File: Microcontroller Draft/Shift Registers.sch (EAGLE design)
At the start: 20 parts, among them IC1 74HC595N, IC2 74HC595N

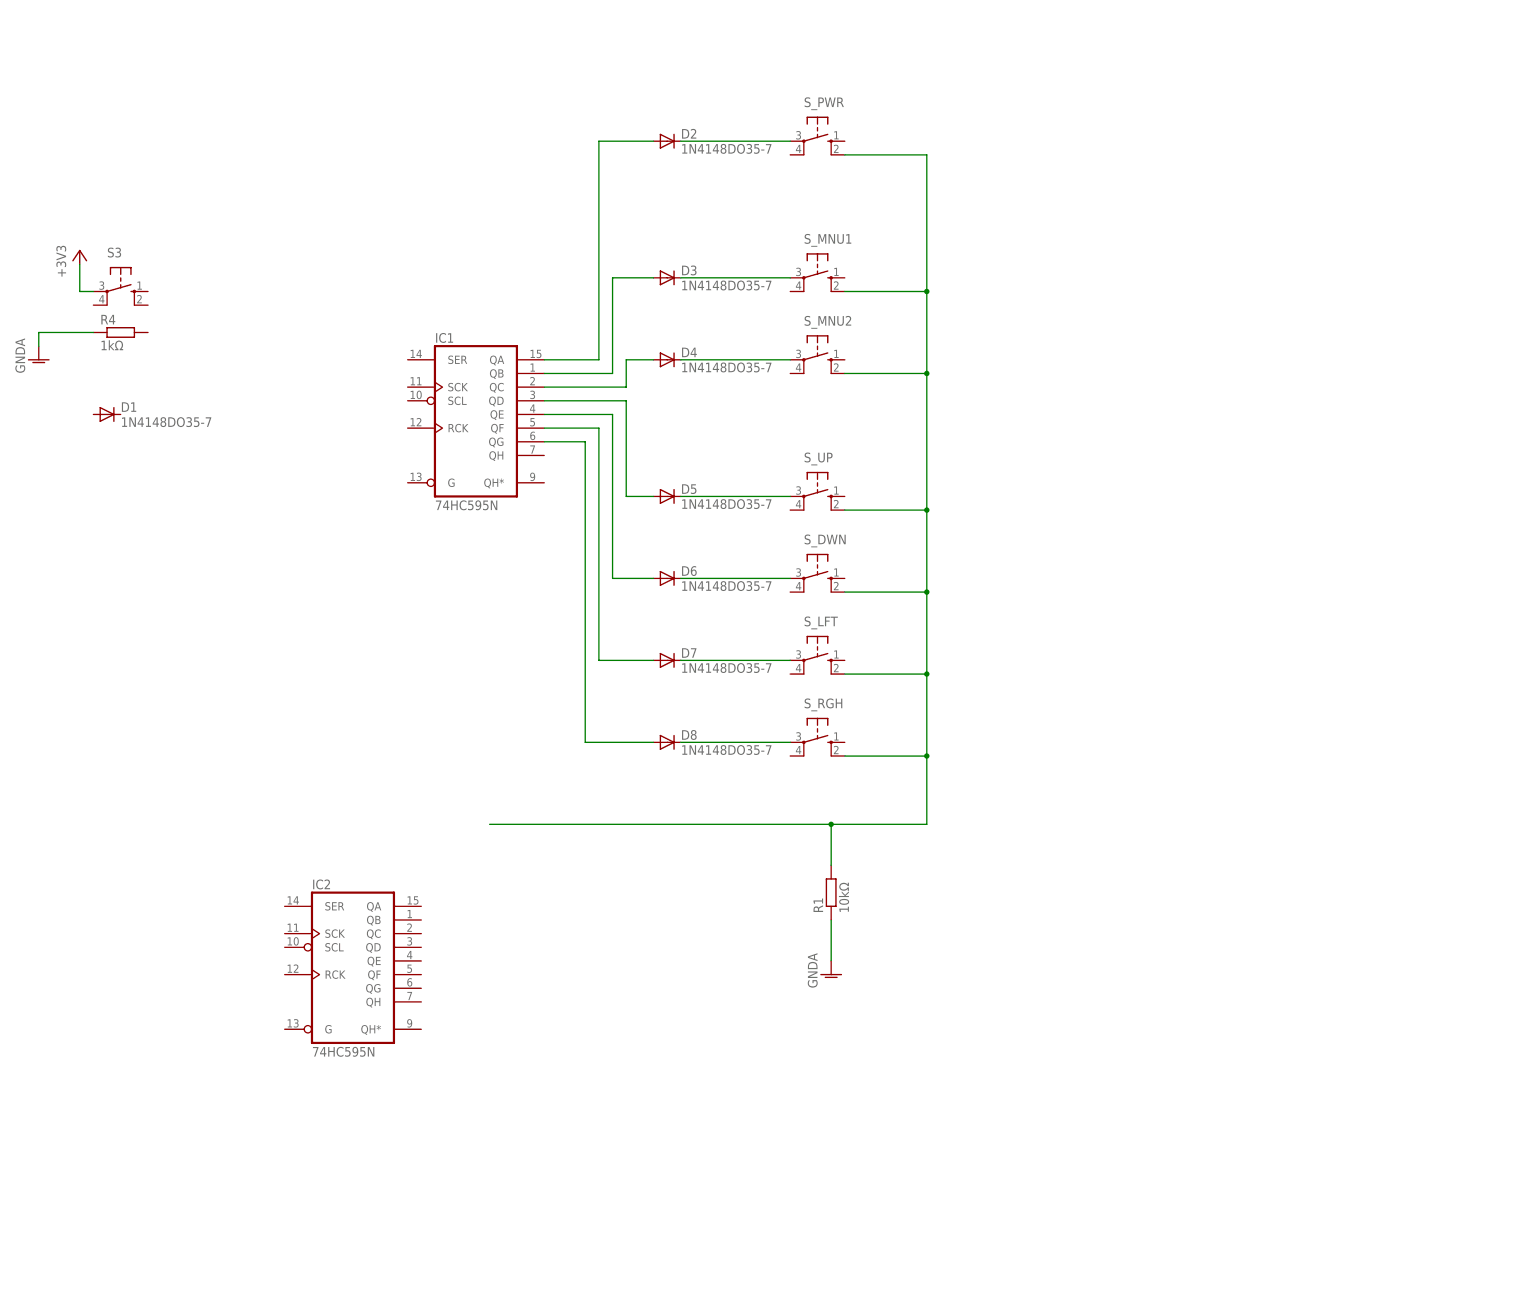
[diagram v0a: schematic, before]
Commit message: Finished the shift register oriented design schematic
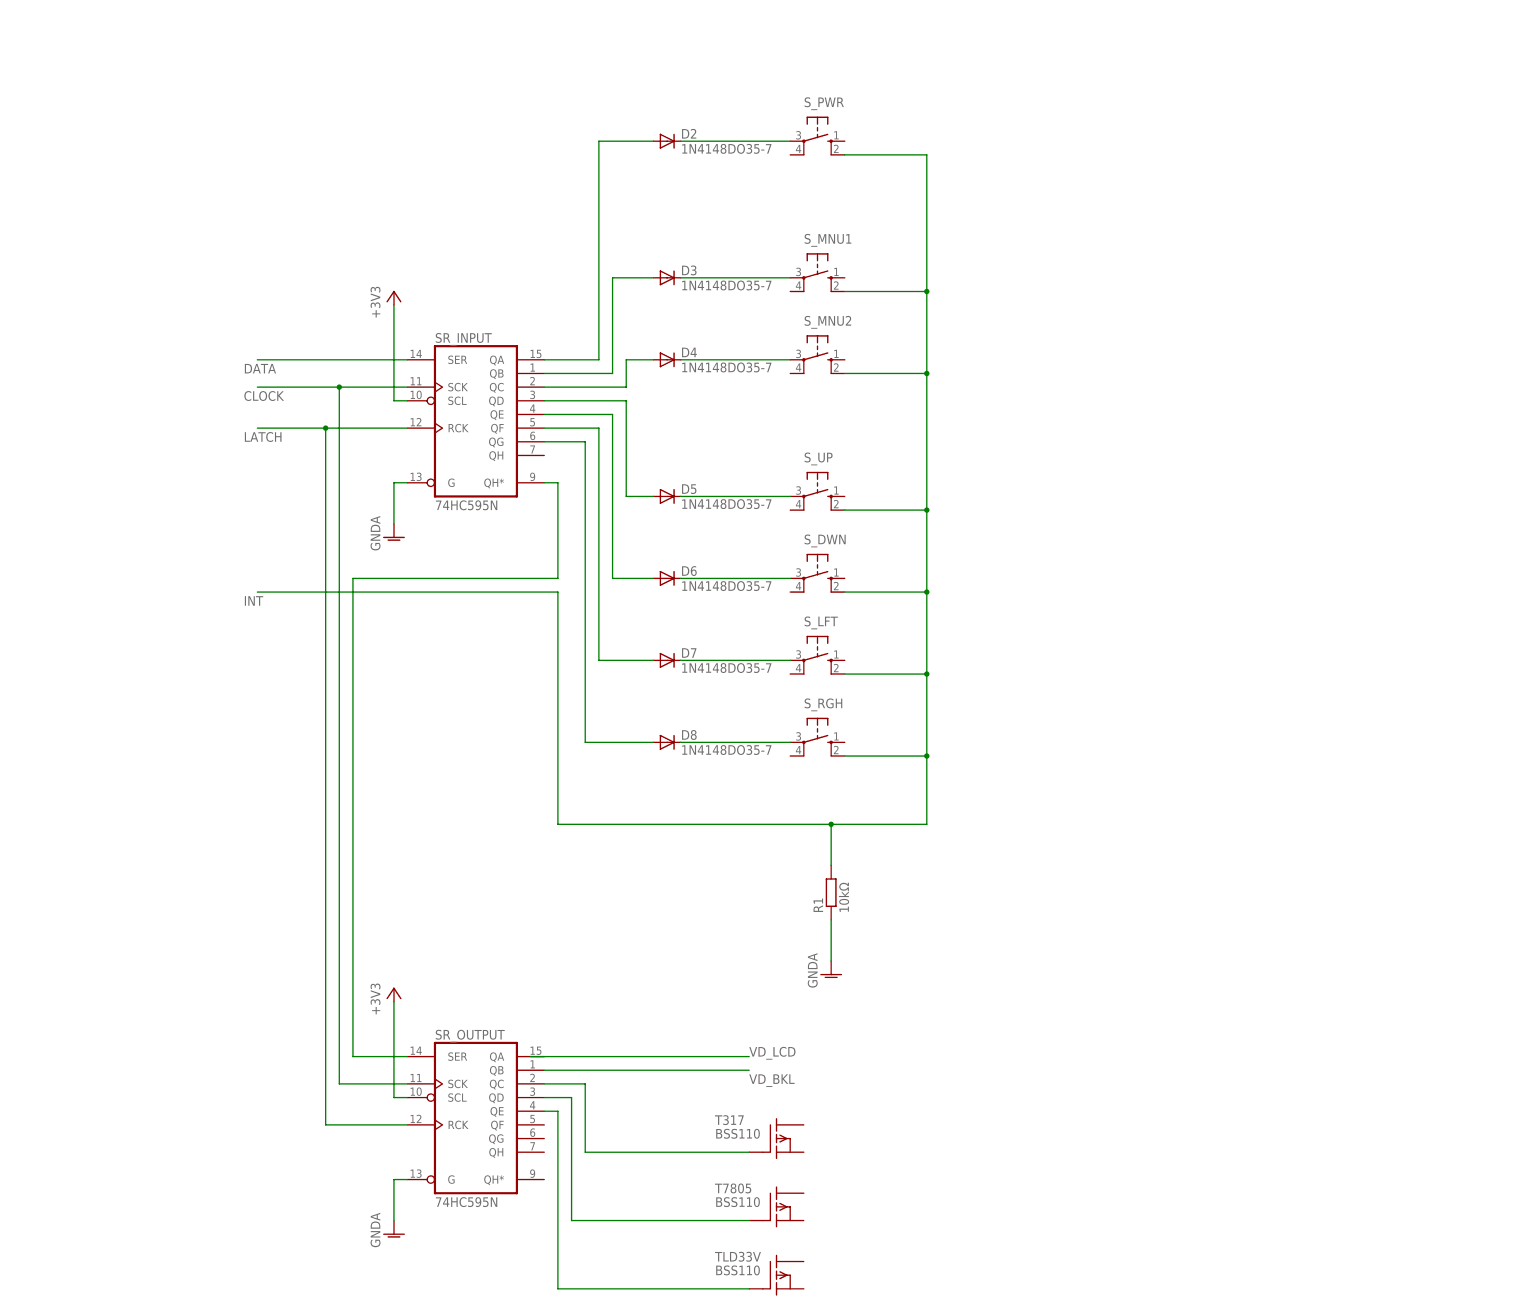
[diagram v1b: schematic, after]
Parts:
- removed D1: 1N4148DO35-7, diode:1N4148DO35-7
- removed IC2: 74HC595N, 74xx-eu:74HC595N
- removed R4: 1kΩ, resistor:R-EU_0207/10
- removed S3: (no value), switch-omron:10-XX
- added SR_OUTPUT: 74HC595N, 74xx-eu:74HC595N
- added T317, T7805, TLD33V: BSS110, transistor-fet:BSS110
- renumbered IC1 to SR_INPUT
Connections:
- net N$1 renamed INT
- new net CLOCK: SR_INPUTA.SCK, SR_OUTPUTA.SCK
- new net DATA: SR_INPUTA.SER
- new net LATCH: SR_INPUTA.RCK, SR_OUTPUTA.RCK
- new net N$19: SR_OUTPUTA.QE, TLD33V.G
- new net N$20: SR_OUTPUTA.QD, T7805.G
- new net N$21: SR_OUTPUTA.QC, T317.G
- new net N$22: SR_INPUTA.QH*, SR_OUTPUTA.SER
- new net VD_BKL: SR_OUTPUTA.QB
- new net VD_LCD: SR_OUTPUTA.QA
- net +3V3: now also SR_INPUTA.SCL, SR_OUTPUTA.SCL; no longer S3.P
- net GNDA: now also SR_INPUTA.G, SR_OUTPUTA.G; no longer R4.1

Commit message: Added some decoupling capacitors
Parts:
- added C1, C7: 0.1uF, rcl:C-EU025-025X050
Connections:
- net +3V3: now also C1.2, C7.2
- net GNDA: now also C1.1, C7.1
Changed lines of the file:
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@@
 <part name="GND3" library="supply1" deviceset="GNDA" device=""/>
 <part name="+3V2" library="supply1" deviceset="+3V3" device=""/>
+<part name="C7" library="rcl" deviceset="C-EU" device="025-025X050" value="0.1uF"/>
+<part name="GND4" library="supply1" deviceset="GNDA" device=""/>
+<part name="C1" library="rcl" deviceset="C-EU" device="025-025X050" value="0.1uF"/>
+<part name="GND5" library="supply1" deviceset="GNDA" device=""/>
 </parts>
 <sheets>
@@
 <instance part="GND3" gate="1" x="-38.1" y="-58.42"/>
 <instance part="+3V2" gate="G$1" x="-38.1" y="-12.7"/>
+<instance part="C7" gate="G$1" x="-50.8" y="111.76" rot="R90"/>
+<instance part="GND4" gate="1" x="-55.88" y="109.22"/>
+<instance part="C1" gate="G$1" x="-58.42" y="-17.78" rot="R90"/>
+<instance part="GND5" gate="1" x="-63.5" y="-22.86"/>
 </instances>
 <busses>
@@
 <segment>
 <pinref part="+3V1" gate="G$1" pin="+3V3"/>
-<wire x1="-38.1" y1="114.3" x2="-38.1" y2="96.52" width="0.1524" layer="91"/>
+<wire x1="-38.1" y1="114.3" x2="-38.1" y2="111.76" width="0.1524" layer="91"/>
 <pinref part="SR_INPUT" gate="A" pin="SCL"/>
+<wire x1="-38.1" y1="111.76" x2="-38.1" y2="96.52" width="0.1524" layer="91"/>
 <wire x1="-38.1" y1="96.52" x2="-35.56" y2="96.52" width="0.1524" layer="91"/>
+<pinref part="C7" gate="G$1" pin="2"/>
+<wire x1="-45.72" y1="111.76" x2="-38.1" y2="111.76" width="0.1524" layer="91"/>
+<junction x="-38.1" y="111.76"/>
 </segment>
 <segment>
@@
 <pinref part="+3V2" gate="G$1" pin="+3V3"/>
 <wire x1="-35.56" y1="-33.02" x2="-38.1" y2="-33.02" width="0.1524" layer="91"/>
-<wire x1="-38.1" y1="-33.02" x2="-38.1" y2="-15.24" width="0.1524" layer="91"/>
+<wire x1="-38.1" y1="-33.02" x2="-38.1" y2="-17.78" width="0.1524" layer="91"/>
+<pinref part="C1" gate="G$1" pin="2"/>
+<wire x1="-38.1" y1="-17.78" x2="-38.1" y2="-15.24" width="0.1524" layer="91"/>
+<wire x1="-53.34" y1="-17.78" x2="-38.1" y2="-17.78" width="0.1524" layer="91"/>
+<junction x="-38.1" y="-17.78"/>
 </segment>
 </net>
@@
 <wire x1="-38.1" y1="-48.26" x2="-38.1" y2="-55.88" width="0.1524" layer="91"/>
 </segment>
+<segment>
+<pinref part="C7" gate="G$1" pin="1"/>
+<wire x1="-53.34" y1="111.76" x2="-55.88" y2="111.76" width="0.1524" layer="91"/>
+<pinref part="GND4" gate="1" pin="GNDA"/>
+</segment>
+<segment>
+<pinref part="C1" gate="G$1" pin="1"/>
+<wire x1="-60.96" y1="-17.78" x2="-63.5" y2="-17.78" width="0.1524" layer="91"/>
+<pinref part="GND5" gate="1" pin="GNDA"/>
+<wire x1="-63.5" y1="-17.78" x2="-63.5" y2="-20.32" width="0.1524" layer="91"/>
+</segment>
 </net>

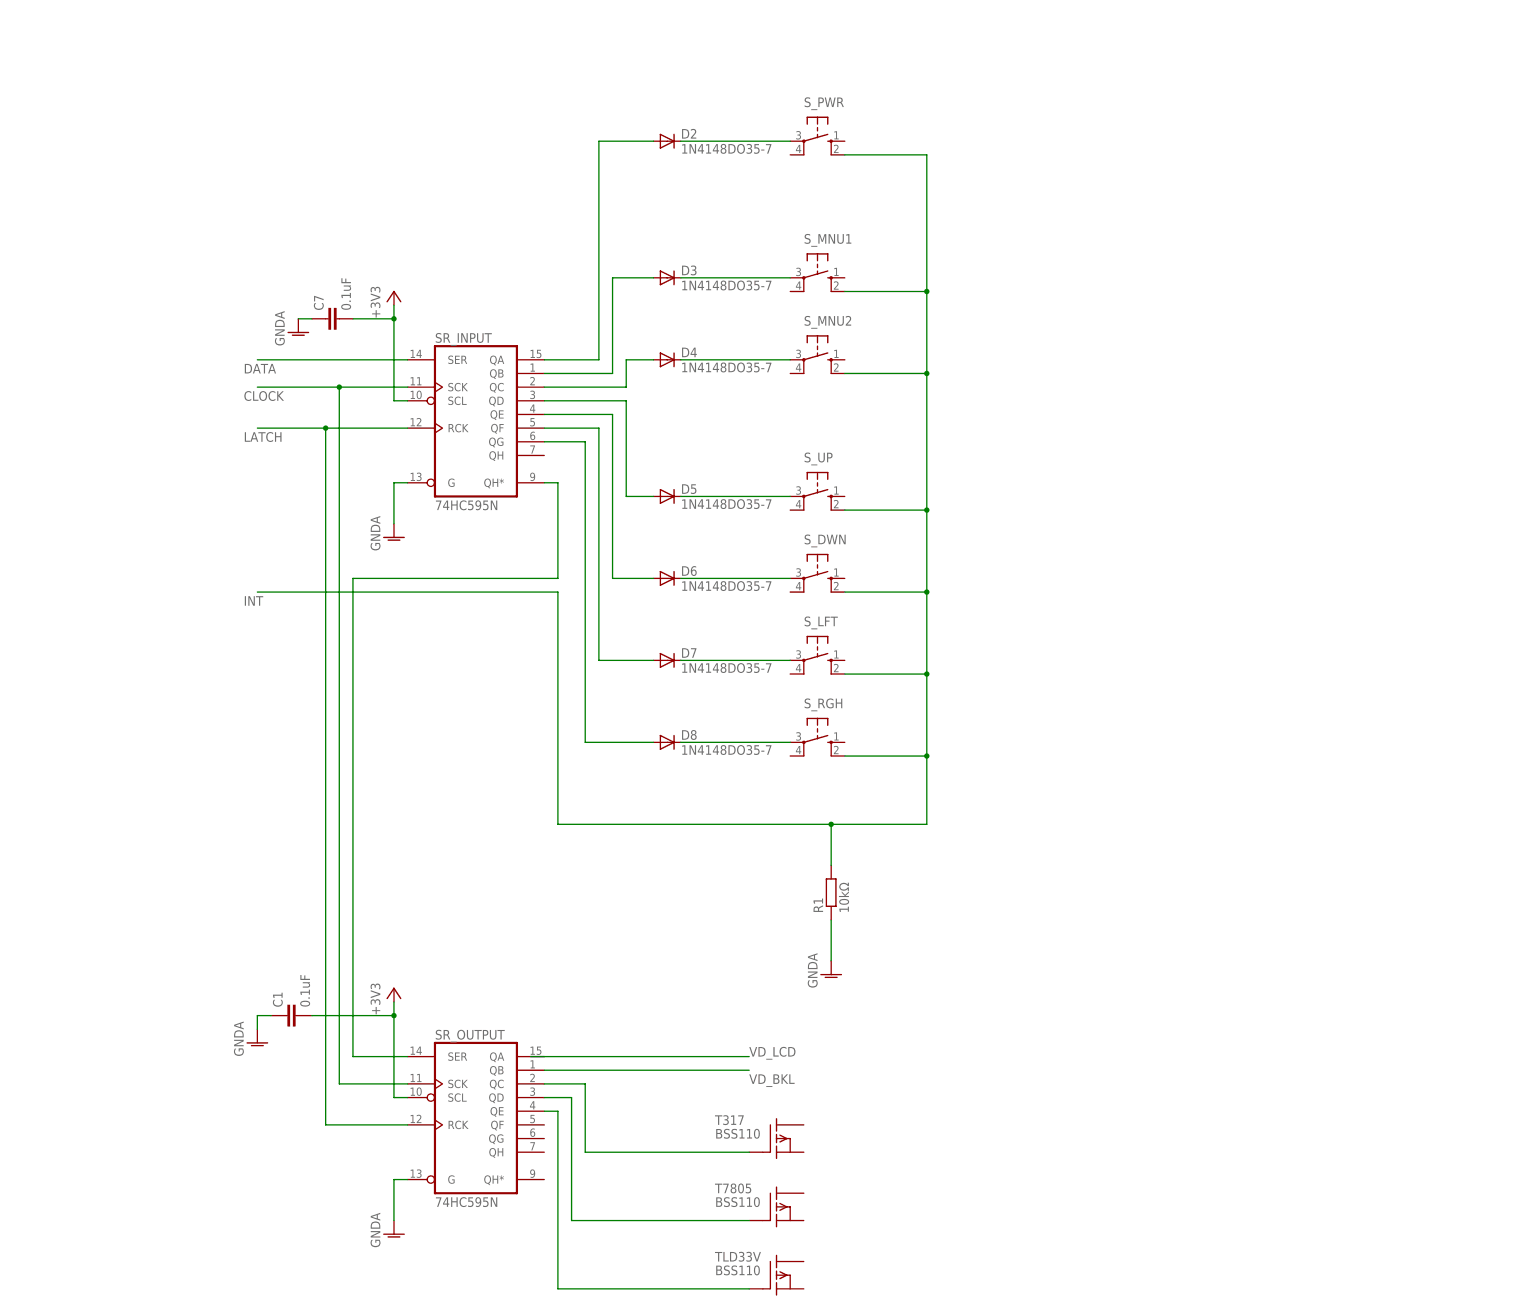
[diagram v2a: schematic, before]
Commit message: Improved the shift register design since we are going to use a rotary encoder
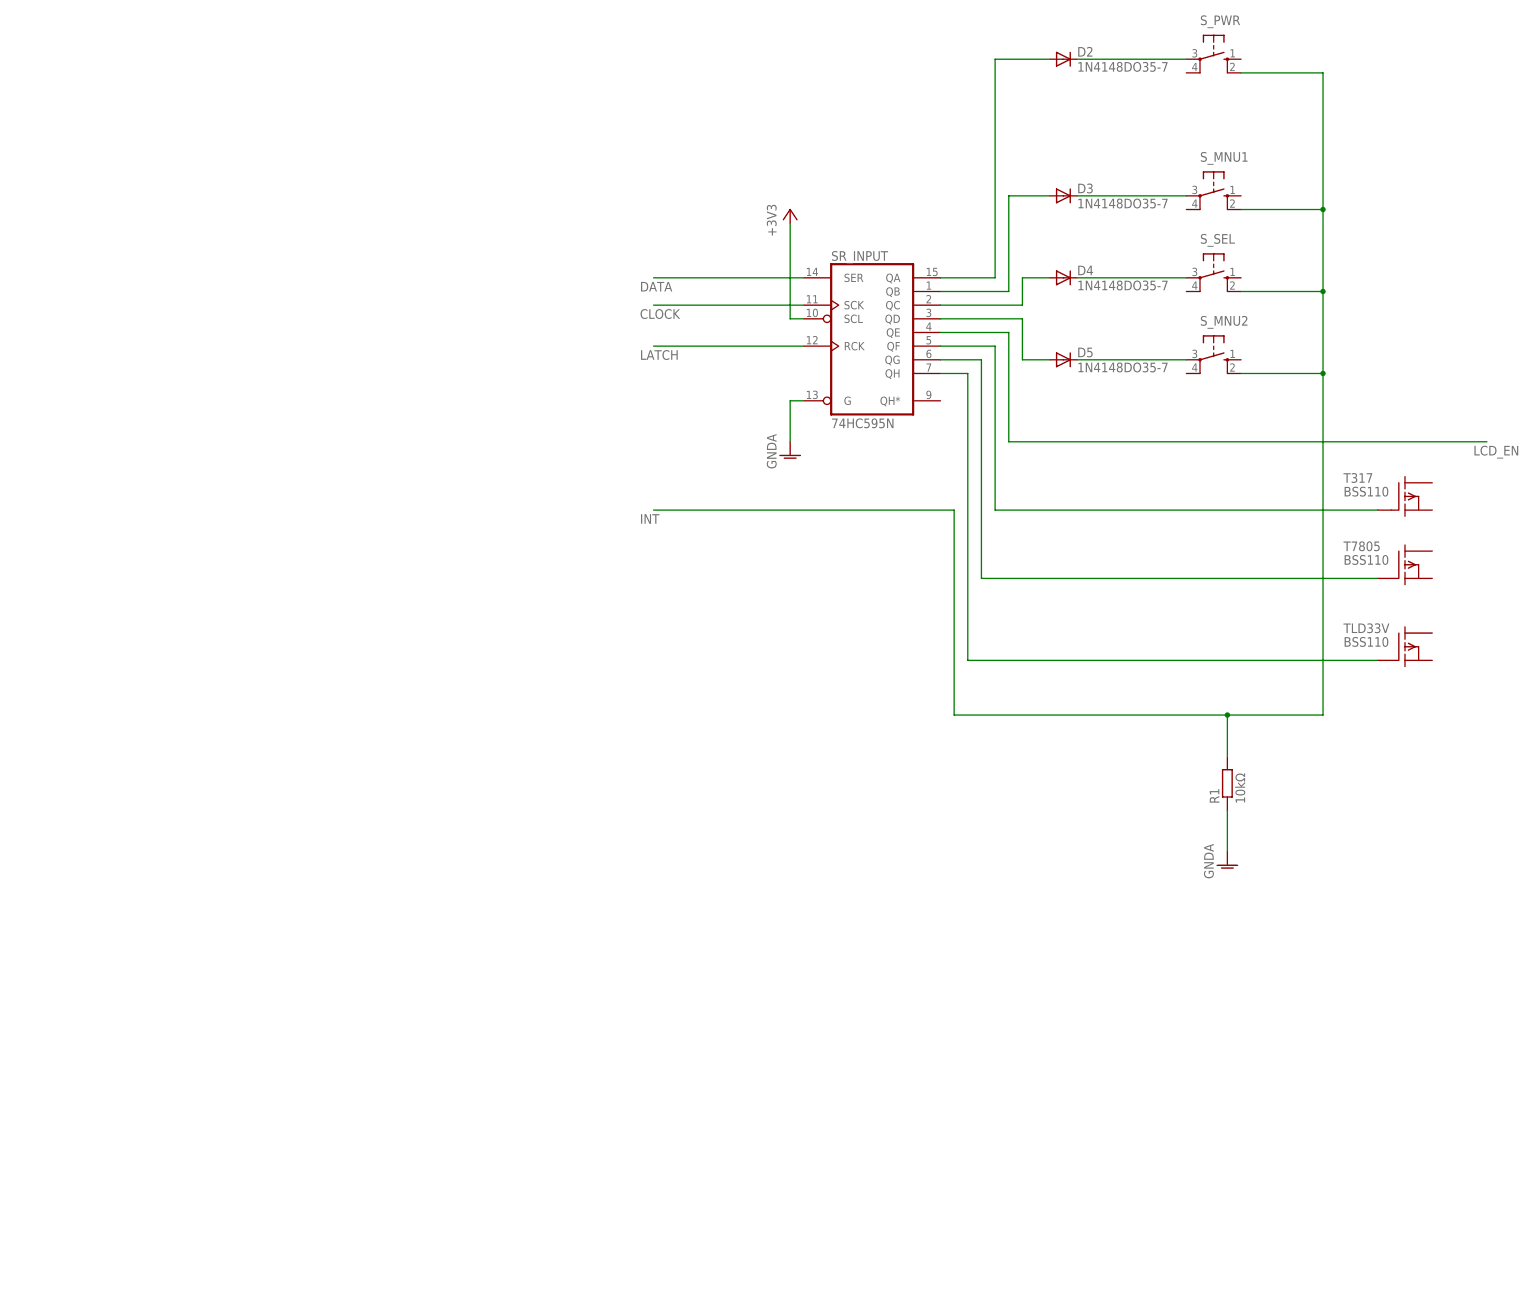
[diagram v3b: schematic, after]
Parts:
- removed C1, C7: 0.1uF, rcl:C-EU025-025X050
- removed D6, D7, D8: 1N4148DO35-7, diode:1N4148DO35-7
- removed SR_OUTPUT: 74HC595N, 74xx-eu:74HC595N
- removed S_DWN, S_LFT, S_RGH, S_UP: (no value), switch-omron:10-XX
- added S_SEL: (no value), switch-omron:10-XX
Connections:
- removed net N$14: D6.A, SR_INPUTA.QE
- removed net N$19: SR_OUTPUTA.QE, TLD33V.G
- removed net N$20: SR_OUTPUTA.QD, T7805.G
- removed net N$21: SR_OUTPUTA.QC, T317.G
- removed net N$22: SR_INPUTA.QH*, SR_OUTPUTA.SER
- removed net N$6: D6.C, S_DWN.P
- removed net N$7: D7.C, S_LFT.P
- removed net N$8: D8.C, S_RGH.P
- removed net VD_BKL: SR_OUTPUTA.QB
- removed net VD_LCD: SR_OUTPUTA.QA
- new net LCD_EN: SR_INPUTA.QE
- new net N$1: SR_INPUTA.QH, TLD33V.G
- net +3V3: no longer C1.2, C7.2, SR_OUTPUTA.SCL
- net CLOCK: no longer SR_OUTPUTA.SCK
- net GNDA: no longer C1.1, C7.1, SR_OUTPUTA.G
- net INT: now also S_SEL.S1; no longer S_DWN.S1, S_LFT.S1, S_RGH.S1, S_UP.S1
- net LATCH: no longer SR_OUTPUTA.RCK
- net N$12: now also T7805.G; no longer D8.A
- net N$13: now also T317.G; no longer D7.A
- net N$4: now also S_SEL.P; no longer S_MNU2.P
- net N$5: now also S_MNU2.P; no longer S_UP.P
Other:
- moved on the sheet: D2, D3, D4, D5, R1, SR_INPUT, S_MNU1, S_MNU2, S_PWR, T317, T7805, TLD33V
